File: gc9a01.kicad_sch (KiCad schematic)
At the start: 6 parts, among them J301 Conn_01x12_Pin, Q301 C42441446

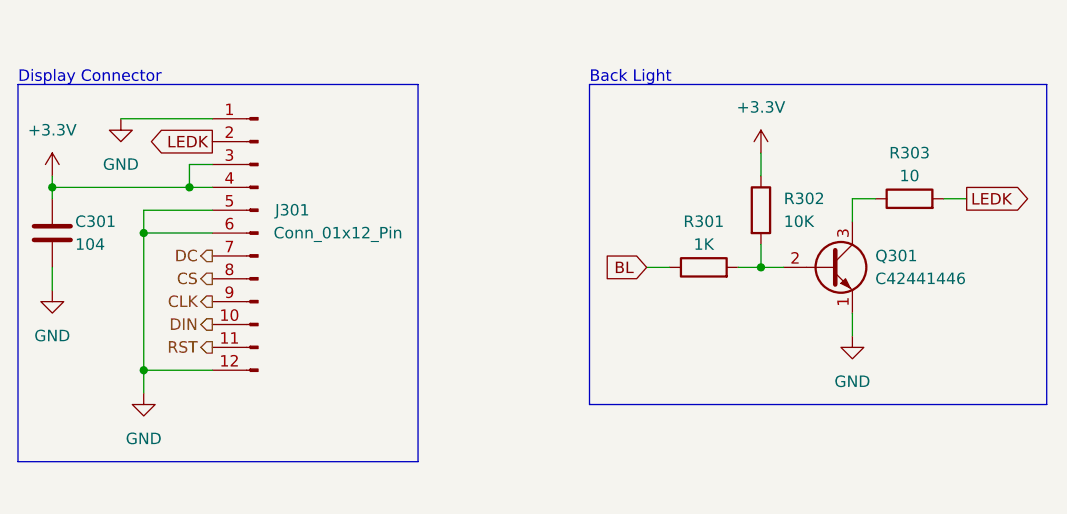
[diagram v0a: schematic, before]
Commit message: Reworked DisplayBoard circuitry and layout; v1.1
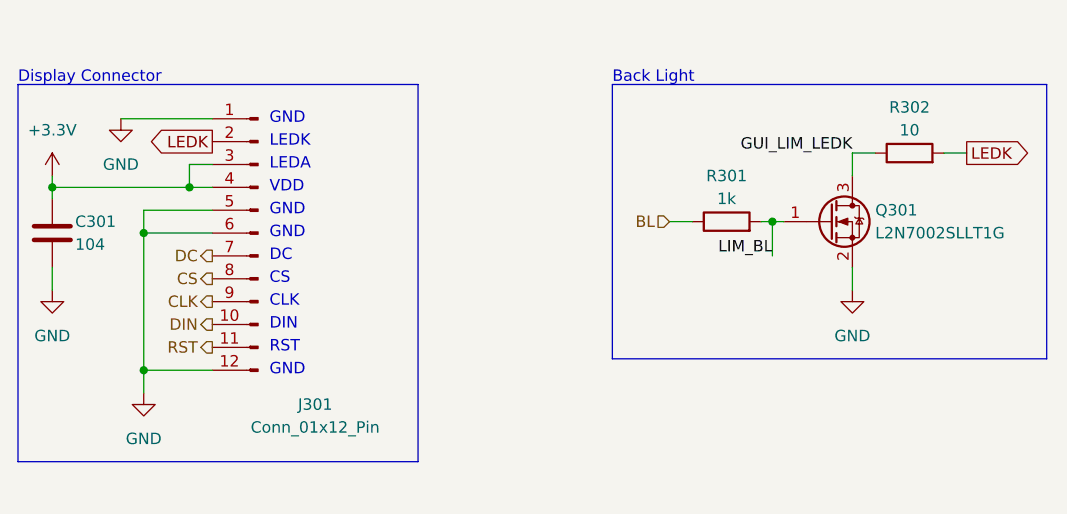
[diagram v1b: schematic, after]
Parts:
- removed Q301: C42441446, Package_TO_SOT_SMD:SOT-23, symbol Transistor_BJT:S8050
- removed R303: 10, Resistor_SMD:R_0603_1608Metric, symbol Device:R
- added Q301: L2N7002SLLT1G, CustomFootprints:SOT_TO_92_L2N7002SLLT1G, symbol CustomSymbols:L2N7002SLLT1G
- J301: footprint CustomFootprints:GC9A01-Connector -> CustomFootprints:GC9A01_Connector
- R301: value 1K -> 1k
- R302: value 10K -> 10
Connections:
- net +3.3V: no longer R302.1
- net GND: now also Q301.2 (S)
- net LEDK: now also R302.2
- net LIM_BL: now reaches R301.2
- net LIM_BL: now also Q301.1 (G); no longer R302.2
- new net GUI_LIM_LEDK: Q301.3 (D), R302.1
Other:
- note added: "CLK"
- note added: "CS"
- note added: "DC"
- note added: "DIN"
- note added: "GND"
- note added: "LEDA"
- note added: "LEDK"
- note added: "RST"
- note added: "VDD"

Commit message: Finished v1.1
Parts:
- removed J301: Conn_01x12_Pin, CustomFootprints:GC9A01_Connector, symbol Connector:Conn_01x12_Pin
- added C6: 100nF, Capacitor_SMD:C_0805_2012Metric, symbol Device:C
- added J2: Conn_01x16, CustomFootprints:ST77916, symbol Connector_Generic:Conn_01x16
- added JP1: SolderJumper_2_Open, Jumper:SolderJumper-2_P1.3mm_Open_Pad1.0x1.5mm, symbol Jumper:SolderJumper_2_Open
- added R8: 100k, Resistor_SMD:R_0603_1608Metric, symbol Device:R
- C7: renamed from C301; value 104 -> 100nF
- Q1: renamed from Q301; value L2N7002SLLT1G -> Si2302CDS-T1-GE3; footprint CustomFootprints:SOT_TO_92_L2N7002SLLT1G -> Package_TO_SOT_SMD:SOT-23
- R7: renamed from R301; value 1k -> 10k
- renumbered R302 to R9
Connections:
- net +3.3V: now also C6.1, J2.12 (Pin_12), J2.13 (Pin_13), J2.2 (Pin_2)
- net CLK: now also J2.5 (Pin_5)
- net CS: now also J2.4 (Pin_4)
- net GND: now also C6.2, J2.14 (Pin_14), J2.15 (Pin_15), J2.16 (Pin_16), J2.3 (Pin_3), JP1.2 (B), R8.1
- net LEDK: now also J2.1 (Pin_1)
- net RST: now also J2.6 (Pin_6)
- net GUI_LIM_LEDK: no longer names the net of Q1.3 (D), R9.1
- net GUI_LIM_LEDK: now also JP1.1 (A)
- net LIM_BL: no longer names the net of Q1.1 (G), R7.2
- net LIM_BL: now also R8.2
- new net IO0: J2.10 (Pin_10)
- new net IO1: J2.9 (Pin_9)
- new net IO2: J2.8 (Pin_8)
- new net IO3: J2.7 (Pin_7)
- new net TE: J2.11 (Pin_11)
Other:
- note added: "IO0"
- note added: "IO1"
- note added: "IO2"
- note added: "IO3"
- note added: "TE"
- note added: "VCC"
- note removed: "DC"
- note removed: "DIN"
- note removed: "VDD"
- moved on the sheet: C7
